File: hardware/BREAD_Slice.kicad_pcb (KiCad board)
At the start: 2 copper layers, 70 x 100 mm, 55 parts, among them J1 1985195, J2 1990106, J3 1990106, J4 Conn_01x10_Socket, Q1 NTGS4111PT1G, SW1 SW_SPDT, SW2 SW_DIP_x04, SW3 SW_DIP_x04, U1 AP63205, U2 LTV-817S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

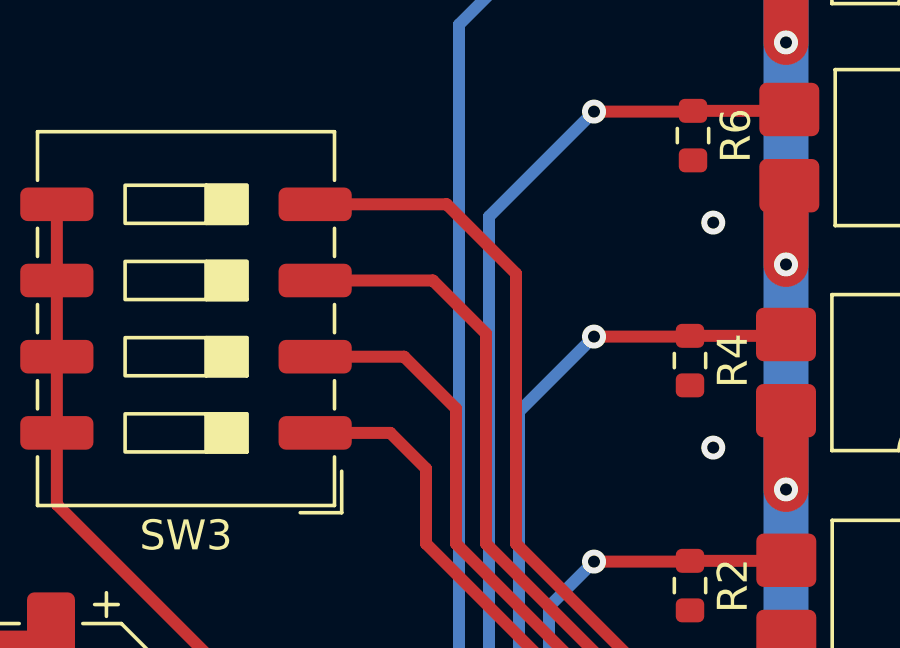
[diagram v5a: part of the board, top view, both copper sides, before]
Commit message: added silkscreen for dip switches
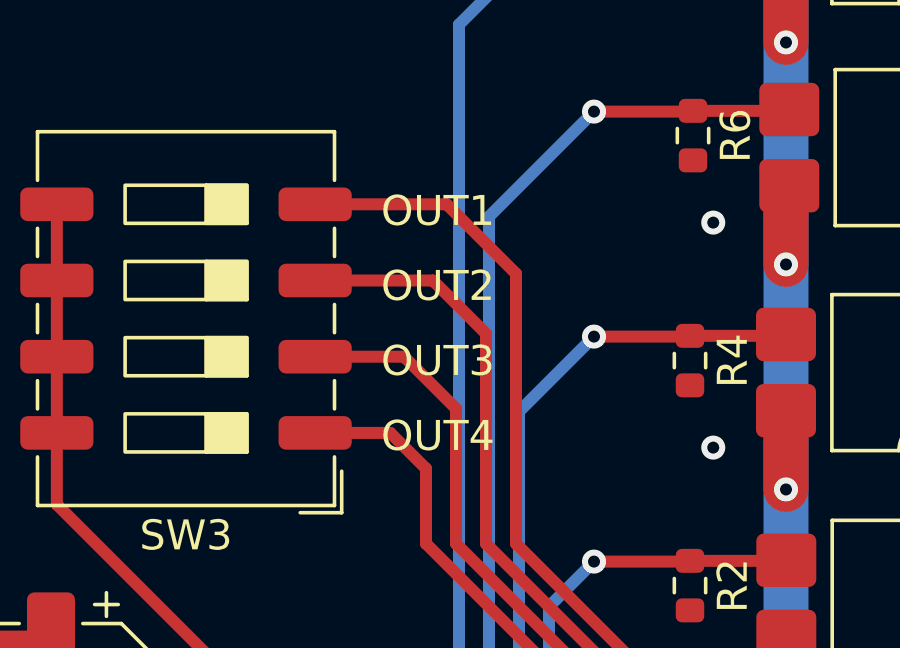
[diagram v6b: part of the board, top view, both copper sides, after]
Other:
- board text added: "OUT1"
- board text added: "OUT2"
- board text added: "OUT3"
- board text added: "OUT4"
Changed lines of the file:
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@@
+		)
+	)
+	(gr_text "OUT1"
+		(at 148.5 67 0)
+		(layer "F.SilkS")
+		(effects
+			(font
+				(size 1 1)
+				(thickness 0.15)
+			)
+			(justify left bottom)
 		)
 	)
@@
 		)
 	)
+	(gr_text "OUT3"
+		(at 148.5 72 0)
+		(layer "F.SilkS")
+		(effects
+			(font
+				(size 1 1)
+				(thickness 0.15)
+			)
+			(justify left bottom)
+		)
+	)
+	(gr_text "OUT2"
+		(at 148.5 69.5 0)
+		(layer "F.SilkS")
+		(effects
+			(font
+				(size 1 1)
+				(thickness 0.15)
+			)
+			(justify left bottom)
+		)
+	)
+	(gr_text "OUT4"
+		(at 148.5 74.5 0)
+		(layer "F.SilkS")
+		(effects
+			(font
+				(size 1 1)
+				(thickness 0.15)
+			)
+			(justify left bottom)
+		)
+	)
